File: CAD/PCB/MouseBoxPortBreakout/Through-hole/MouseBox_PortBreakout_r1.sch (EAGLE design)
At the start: 7 parts

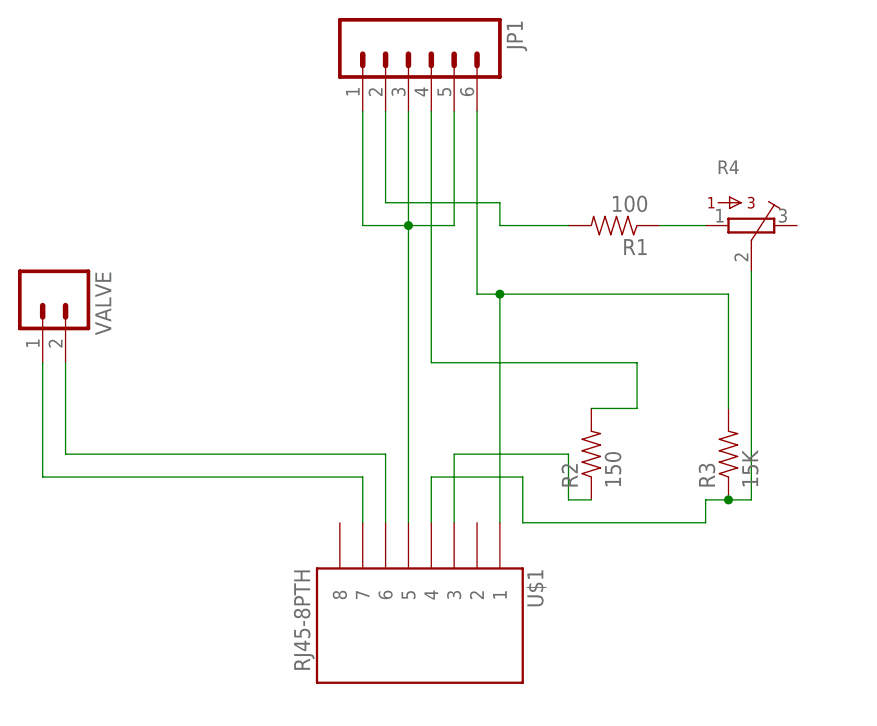
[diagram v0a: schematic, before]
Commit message: -Updated design for mouse box port breakout board -Added a surface mount version of the port breakout board
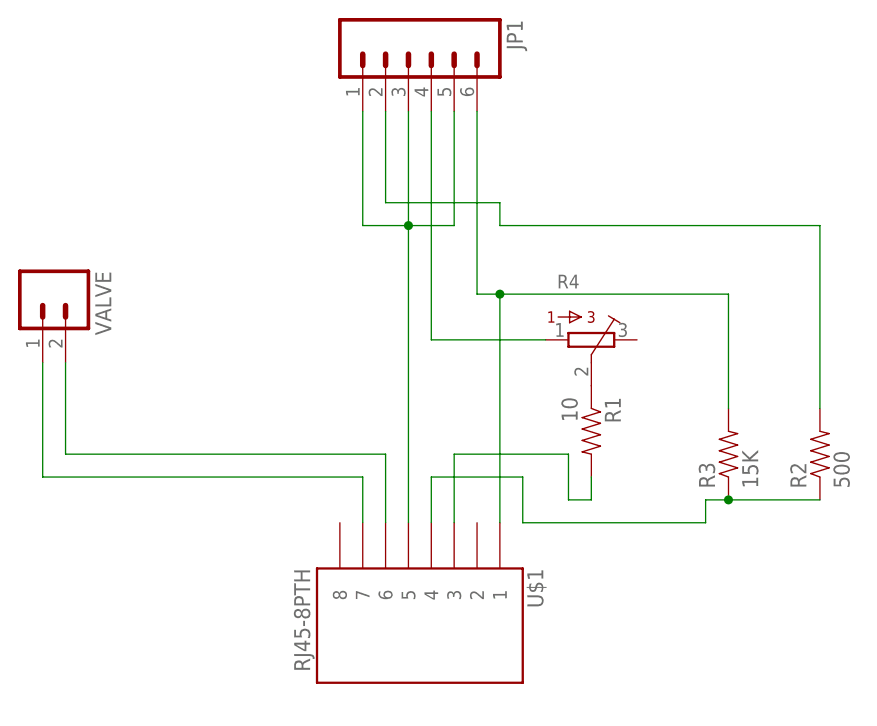
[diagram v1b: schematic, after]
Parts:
- R1: value 100 -> 10
- R2: value 150 -> 500
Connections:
- removed net N$9: R1.1, R4.1
- new net N$4: R1.1, R4.2
- net N$2: now also R2.1; no longer R4.2
- net N$3: now also R2.2; no longer R1.2
- net N$7: now also R4.1; no longer R2.2
- net N$8: now also R1.2; no longer R2.1
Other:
- moved on the sheet: R1, R2, R4
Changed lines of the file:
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@@
 <part name="VALVE" library="SparkFun" deviceset="M02" device="3.5MM_LOCK"/>
 <part name="R4" library="bourns" deviceset="3362" device="R"/>
-<part name="R1" library="SparkFun-Resistors" deviceset="RESISTOR" device="AXIAL-0.3" value="100"/>
-<part name="R2" library="SparkFun-Resistors" deviceset="RESISTOR" device="AXIAL-0.3" value="150"/>
+<part name="R1" library="SparkFun-Resistors" deviceset="RESISTOR" device="AXIAL-0.3" value="10"/>
 <part name="R3" library="SparkFun-Resistors" deviceset="RESISTOR" device="AXIAL-0.3" value="15K"/>
+<part name="R2" library="SparkFun-Resistors" deviceset="RESISTOR" device="AXIAL-0.3" value="500"/>
 </parts>
 <sheets>
@@
 <instance part="JP1" gate="G$1" x="81.28" y="63.5" rot="R270"/>
 <instance part="VALVE" gate="G$1" x="40.64" y="38.1" rot="R270"/>
-<instance part="R4" gate="G$1" x="119.38" y="45.72" rot="R270"/>
-<instance part="R1" gate="G$1" x="104.14" y="45.72" rot="R180"/>
-<instance part="R2" gate="G$1" x="101.6" y="20.32" rot="R90"/>
+<instance part="R4" gate="G$1" x="101.6" y="33.02" rot="R270"/>
+<instance part="R1" gate="G$1" x="101.6" y="22.86" rot="R270"/>
 <instance part="R3" gate="G$1" x="116.84" y="20.32" rot="R90"/>
+<instance part="R2" gate="G$1" x="127" y="20.32" rot="R90"/>
 </instances>
 <busses>
@@
 <segment>
 <wire x1="114.3" y1="15.24" x2="116.84" y2="15.24" width="0.1524" layer="91"/>
-<wire x1="116.84" y1="15.24" x2="119.38" y2="15.24" width="0.1524" layer="91"/>
-<wire x1="119.38" y1="15.24" x2="119.38" y2="40.64" width="0.1524" layer="91"/>
 <wire x1="114.3" y1="15.24" x2="114.3" y2="12.7" width="0.1524" layer="91"/>
 <wire x1="114.3" y1="12.7" x2="93.98" y2="12.7" width="0.1524" layer="91"/>
@@
 <wire x1="83.82" y1="17.78" x2="83.82" y2="12.7" width="0.1524" layer="91"/>
 <pinref part="U$1" gate="G$1" pin="4"/>
-<pinref part="R4" gate="G$1" pin="2"/>
 <pinref part="R3" gate="G$1" pin="1"/>
 <junction x="116.84" y="15.24"/>
+<pinref part="R2" gate="G$1" pin="1"/>
+<wire x1="116.84" y1="15.24" x2="127" y2="15.24" width="0.1524" layer="91"/>
 </segment>
 </net>
@@
 <wire x1="78.74" y1="58.42" x2="78.74" y2="48.26" width="0.1524" layer="91"/>
 <pinref part="JP1" gate="G$1" pin="2"/>
-<pinref part="R1" gate="G$1" pin="2"/>
-<wire x1="99.06" y1="45.72" x2="91.44" y2="45.72" width="0.1524" layer="91"/>
 <wire x1="91.44" y1="45.72" x2="91.44" y2="48.26" width="0.1524" layer="91"/>
 <wire x1="91.44" y1="48.26" x2="78.74" y2="48.26" width="0.1524" layer="91"/>
+<pinref part="R2" gate="G$1" pin="2"/>
+<wire x1="127" y1="25.4" x2="127" y2="45.72" width="0.1524" layer="91"/>
+<wire x1="127" y1="45.72" x2="91.44" y2="45.72" width="0.1524" layer="91"/>
 </segment>
 </net>
@@
 <net name="N$7" class="0">
 <segment>
-<wire x1="83.82" y1="30.48" x2="106.68" y2="30.48" width="0.1524" layer="91"/>
-<wire x1="106.68" y1="30.48" x2="106.68" y2="25.4" width="0.1524" layer="91"/>
-<wire x1="83.82" y1="58.42" x2="83.82" y2="30.48" width="0.1524" layer="91"/>
+<wire x1="83.82" y1="58.42" x2="83.82" y2="33.02" width="0.1524" layer="91"/>
 <pinref part="JP1" gate="G$1" pin="4"/>
-<pinref part="R2" gate="G$1" pin="2"/>
-<wire x1="106.68" y1="25.4" x2="101.6" y2="25.4" width="0.1524" layer="91"/>
+<pinref part="R4" gate="G$1" pin="1"/>
+<wire x1="96.52" y1="33.02" x2="83.82" y2="33.02" width="0.1524" layer="91"/>
 </segment>
 </net>
@@
 <wire x1="86.36" y1="20.32" x2="86.36" y2="12.7" width="0.1524" layer="91"/>
 <pinref part="U$1" gate="G$1" pin="3"/>
-<pinref part="R2" gate="G$1" pin="1"/>
+<pinref part="R1" gate="G$1" pin="2"/>
+<wire x1="101.6" y1="15.24" x2="101.6" y2="17.78" width="0.1524" layer="91"/>
 </segment>
 </net>
-<net name="N$9" class="0">
+<net name="N$4" class="0">
 <segment>
-<pinref part="R4" gate="G$1" pin="1"/>
+<pinref part="R4" gate="G$1" pin="2"/>
 <pinref part="R1" gate="G$1" pin="1"/>
-<wire x1="114.3" y1="45.72" x2="109.22" y2="45.72" width="0.1524" layer="91"/>
 </segment>
 </net>
